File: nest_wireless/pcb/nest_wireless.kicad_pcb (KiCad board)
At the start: 2 copper layers, 143.4 x 111.8 mm, 78 parts, among them J3 Conn_01x04, SW1 SW_PUSH, SW10 SW_PUSH, SW11 SW_PUSH, SW12 SW_PUSH, SW13 SW_PUSH, SW14 SW_PUSH, SW15 SW_PUSH, SW16 SW_PUSH, SW17 SW_PUSH, SW18 SW_PUSH, SW19 SW_PUSH, SW2 SW_PUSH, SW20 SW_PUSH, SW21 SW_PUSH, SW22 SW_PUSH, SW23 SW_PUSH, SW24 SW_PUSH, SW25 Rotary_Encoder_Switch-Device, SW26 SW_PUSH, SW27 SW_PUSH, SW28 SW_PUSH, SW29 SW_PUSH, SW3 SW_PUSH, SW30 SW_PUSH, SW4 SW_PUSH, SW5 SW_PUSH, SW6 SW_PUSH, SW7 SW_PUSH, SW8 SW_PUSH, SW9 SW_PUSH, U2 kb2040

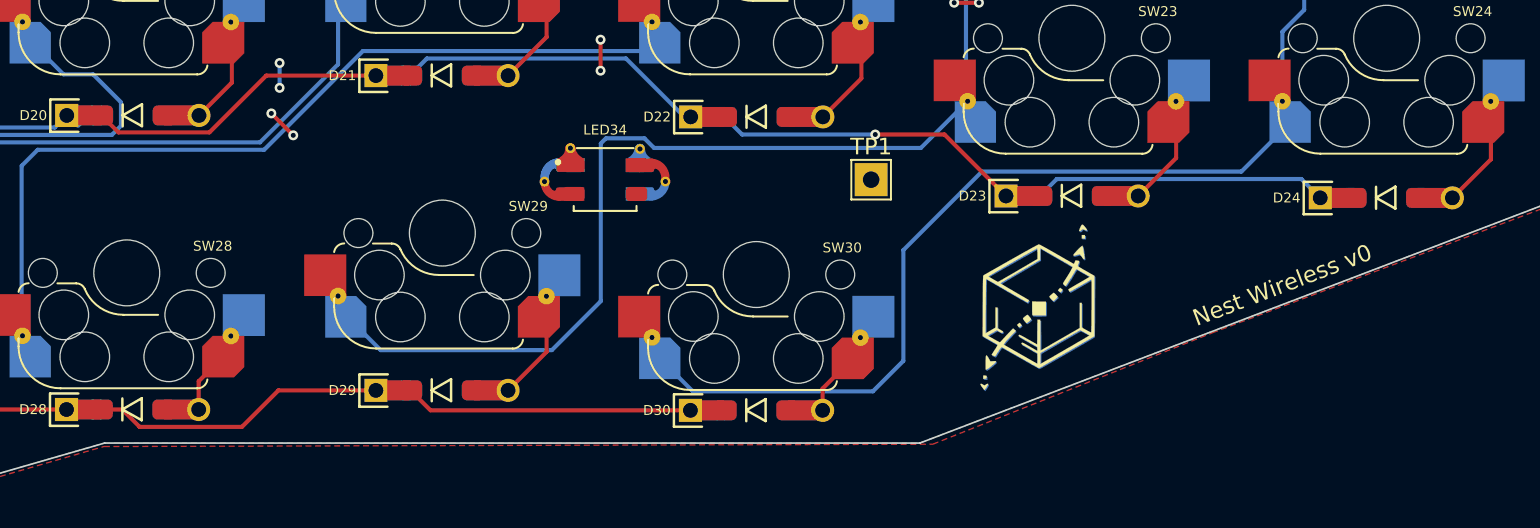
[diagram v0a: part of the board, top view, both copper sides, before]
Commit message: Clean up a few design rule violations
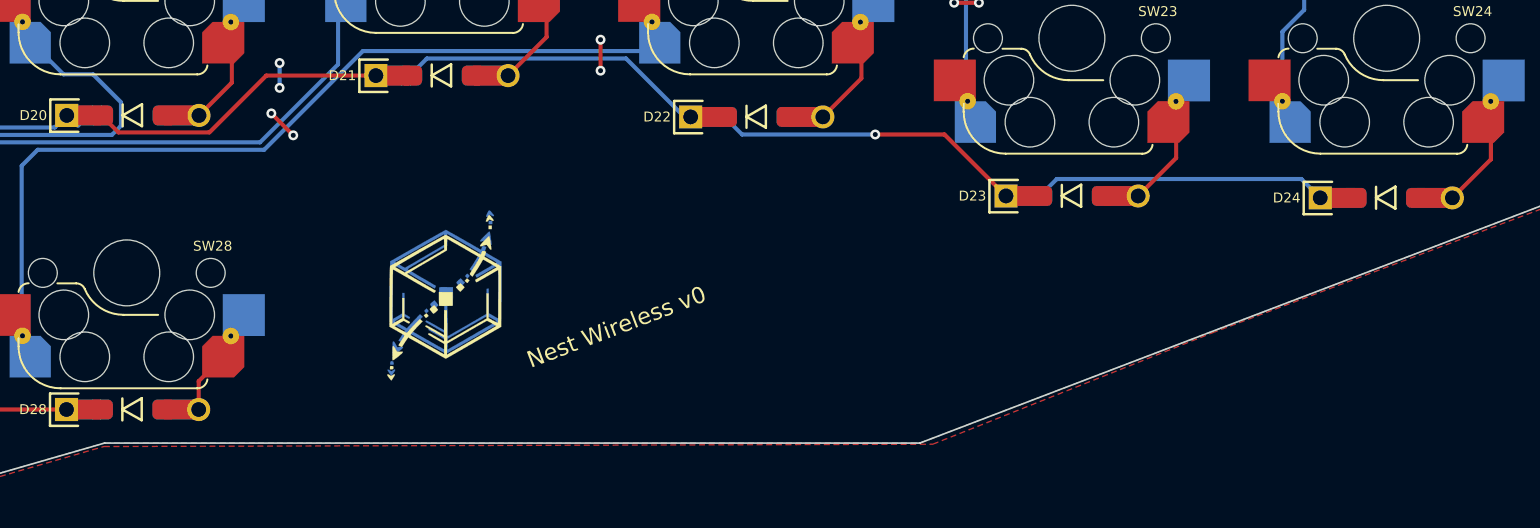
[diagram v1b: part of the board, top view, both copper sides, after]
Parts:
- removed D29, D30: D, NestWireless:D_SOD-123_DO-35_Hybrid_DoubleSided_V2
- removed LED34: SK6803 MINI, NestWireless:SK6812_MINI
- removed SW29, SW30: SW_PUSH, NestWireless:Cherry_MX_DS_Hotswap_v3.5.4
- removed TP1: TestPoint, TestPoint:TestPoint_THTPad_2.0x2.0mm_Drill1.0mm
- moved Ref** 35.9 mm to (158.8, 125.0)
- moved REF** 35.9 mm to (158.9, 125.4)
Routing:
- net col1: track 237.1 -> 186.2 mm
- net col0: track 248.1 -> 197.4 mm
- net row4: track 184.0 -> 148.6 mm
- net Net-(D29-A): track 6.77 -> 0.00 mm
- net Net-(D30-A): track 5.80 -> 0.00 mm

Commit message: Nest wireless kicad project cleanup
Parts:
- removed D25: D, NestWireless:D_SOD-123_DO-35_Hybrid_DoubleSided_V2
- removed SW25: Rotary_Encoder_Switch-Device, NestWireless:RotaryEncoder_Alps_EC11E-Switch_Vertical_H20mm-keebio_modified_hotswap
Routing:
- net SW25B: track 27.3 -> 0.00 mm
- net row4: track 148.6 -> 131.8 mm
